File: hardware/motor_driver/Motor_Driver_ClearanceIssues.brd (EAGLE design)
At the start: 93.7 x 72.4 mm, 88 parts

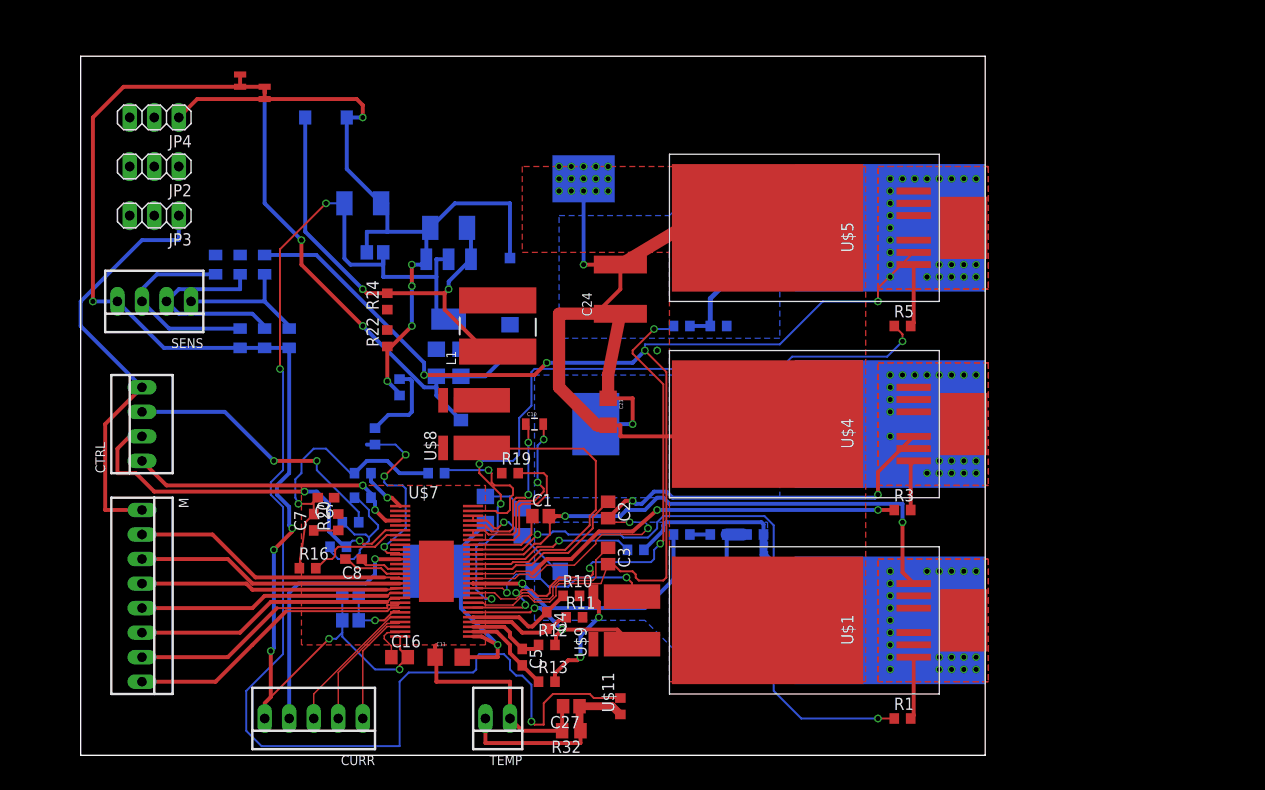
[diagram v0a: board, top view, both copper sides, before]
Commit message: Added Up to date board with ~300 clearence and overlap issues to be opened as a challenge to the general EcoCar Team
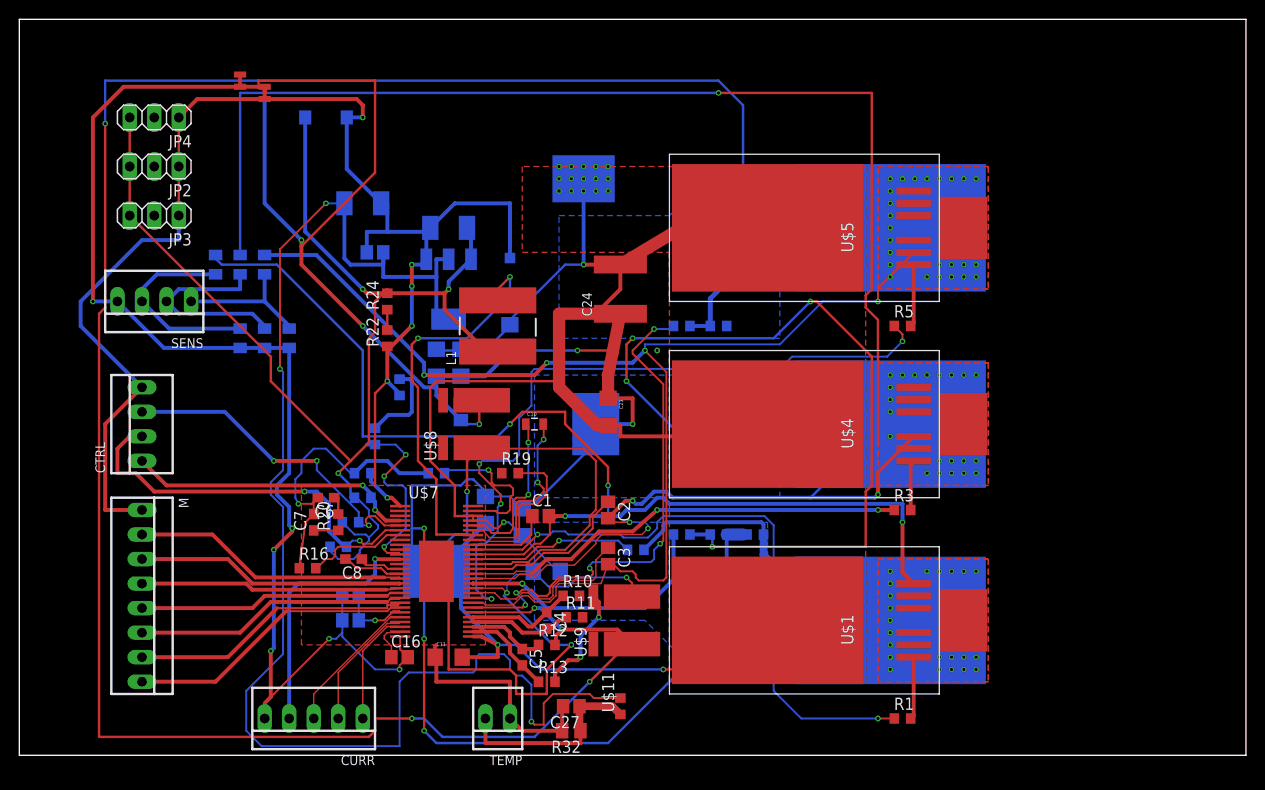
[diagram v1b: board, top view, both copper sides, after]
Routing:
- net H3_LOW: track 19.9 -> 225.7 mm, vias 2 -> 5
- net H2_VS: track 62.9 -> 193.7 mm, vias 4 -> 5
- net GND: track 98.4 -> 223.3 mm, vias 5 -> 9
- net N$3: track 1.69 -> 88.4 mm, vias 0 -> 4
- net VCC: track 107.3 -> 191.1 mm, vias 4 -> 5
- net H1_LOW: track 40.4 -> 111.3 mm, vias 0 -> 3
- net +5V: track 61.1 -> 131.2 mm, vias 2 -> 3
- net H1_VS: track 57.3 -> 120.4 mm, vias 2 -> 4
- net N$19: track 19.0 -> 61.4 mm, vias 2 -> 4
- net DGND: track 182.0 -> 203.4 mm
- net OCTW: track 28.4 -> 34.4 mm, vias 2 -> 3
- net N$20: track 0.00 -> 2.11 mm
- net N$28: track 0.00 -> 2.11 mm
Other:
- board size 93.7 x 72.4 mm -> 127 x 76.2 mm
